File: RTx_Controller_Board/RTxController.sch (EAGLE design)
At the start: 73 parts

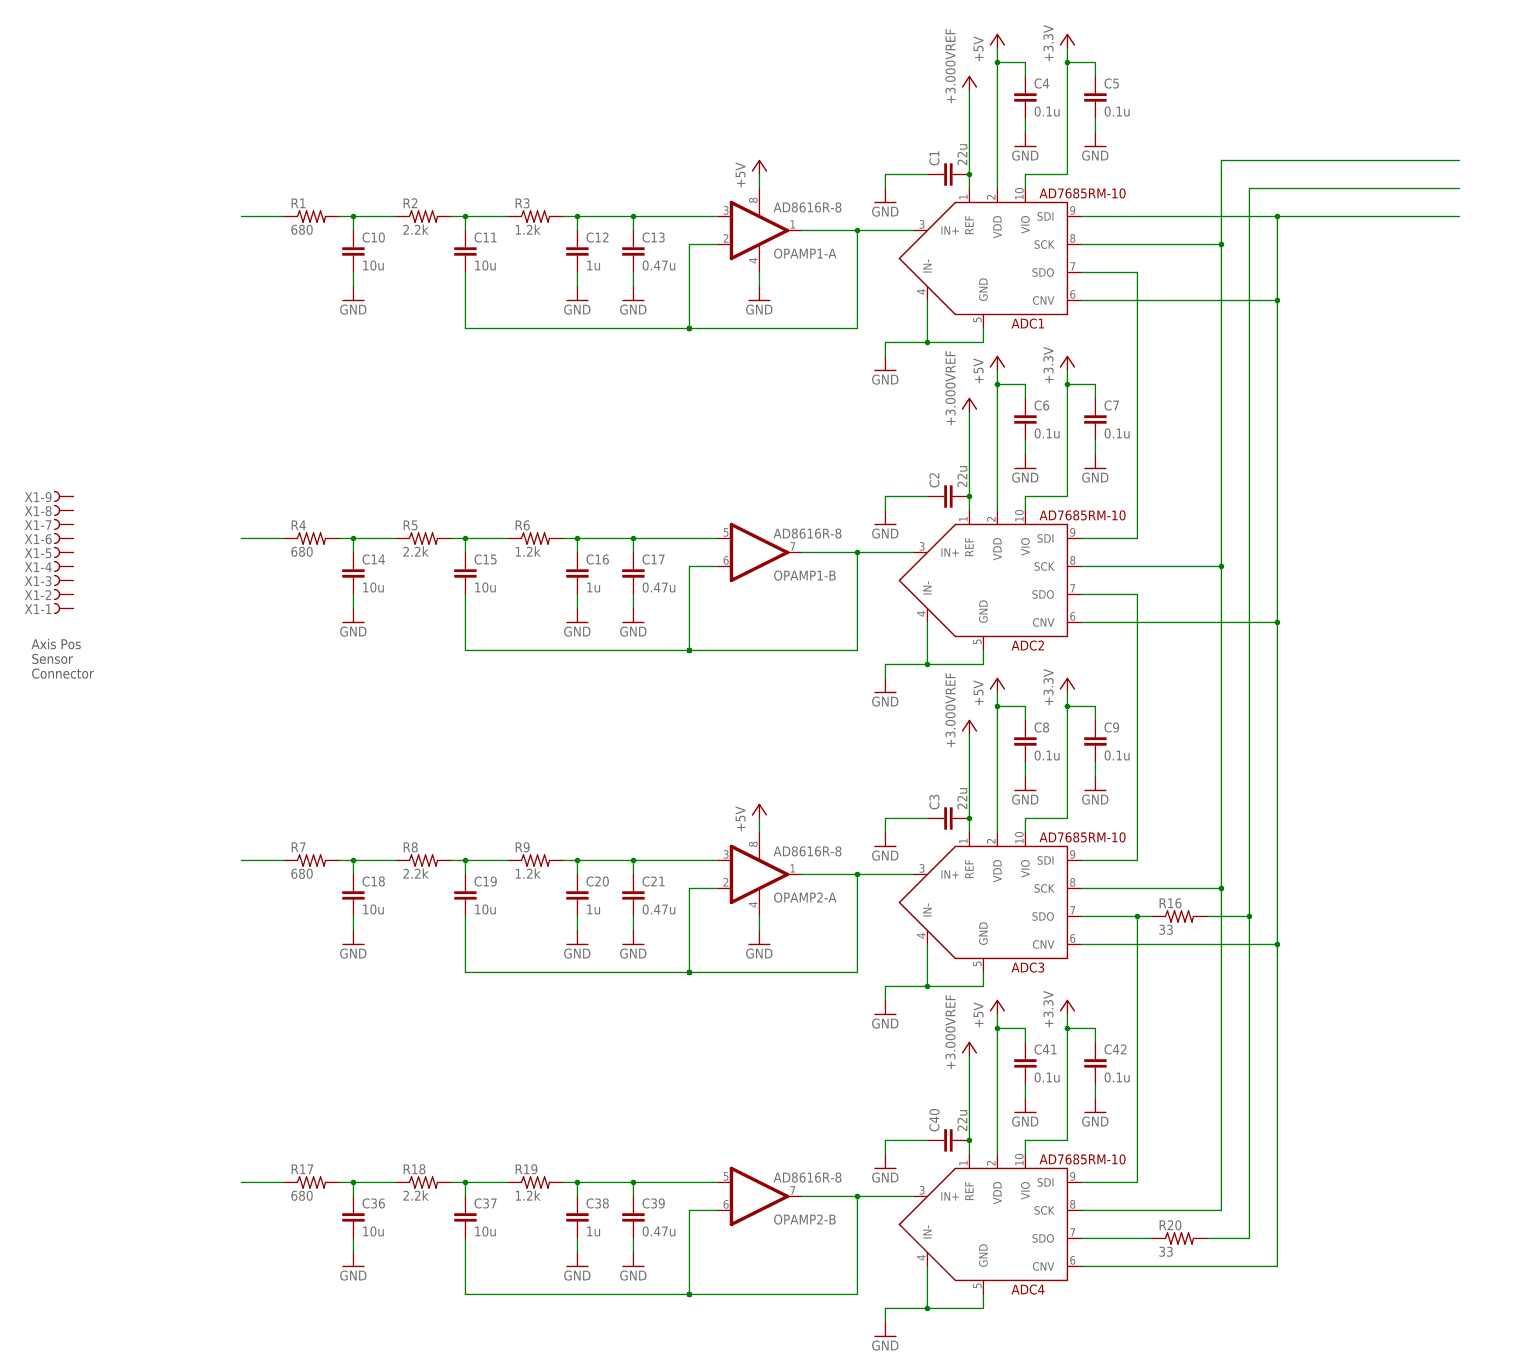
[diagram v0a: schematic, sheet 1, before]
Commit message: Changed ARef to 5.000V.
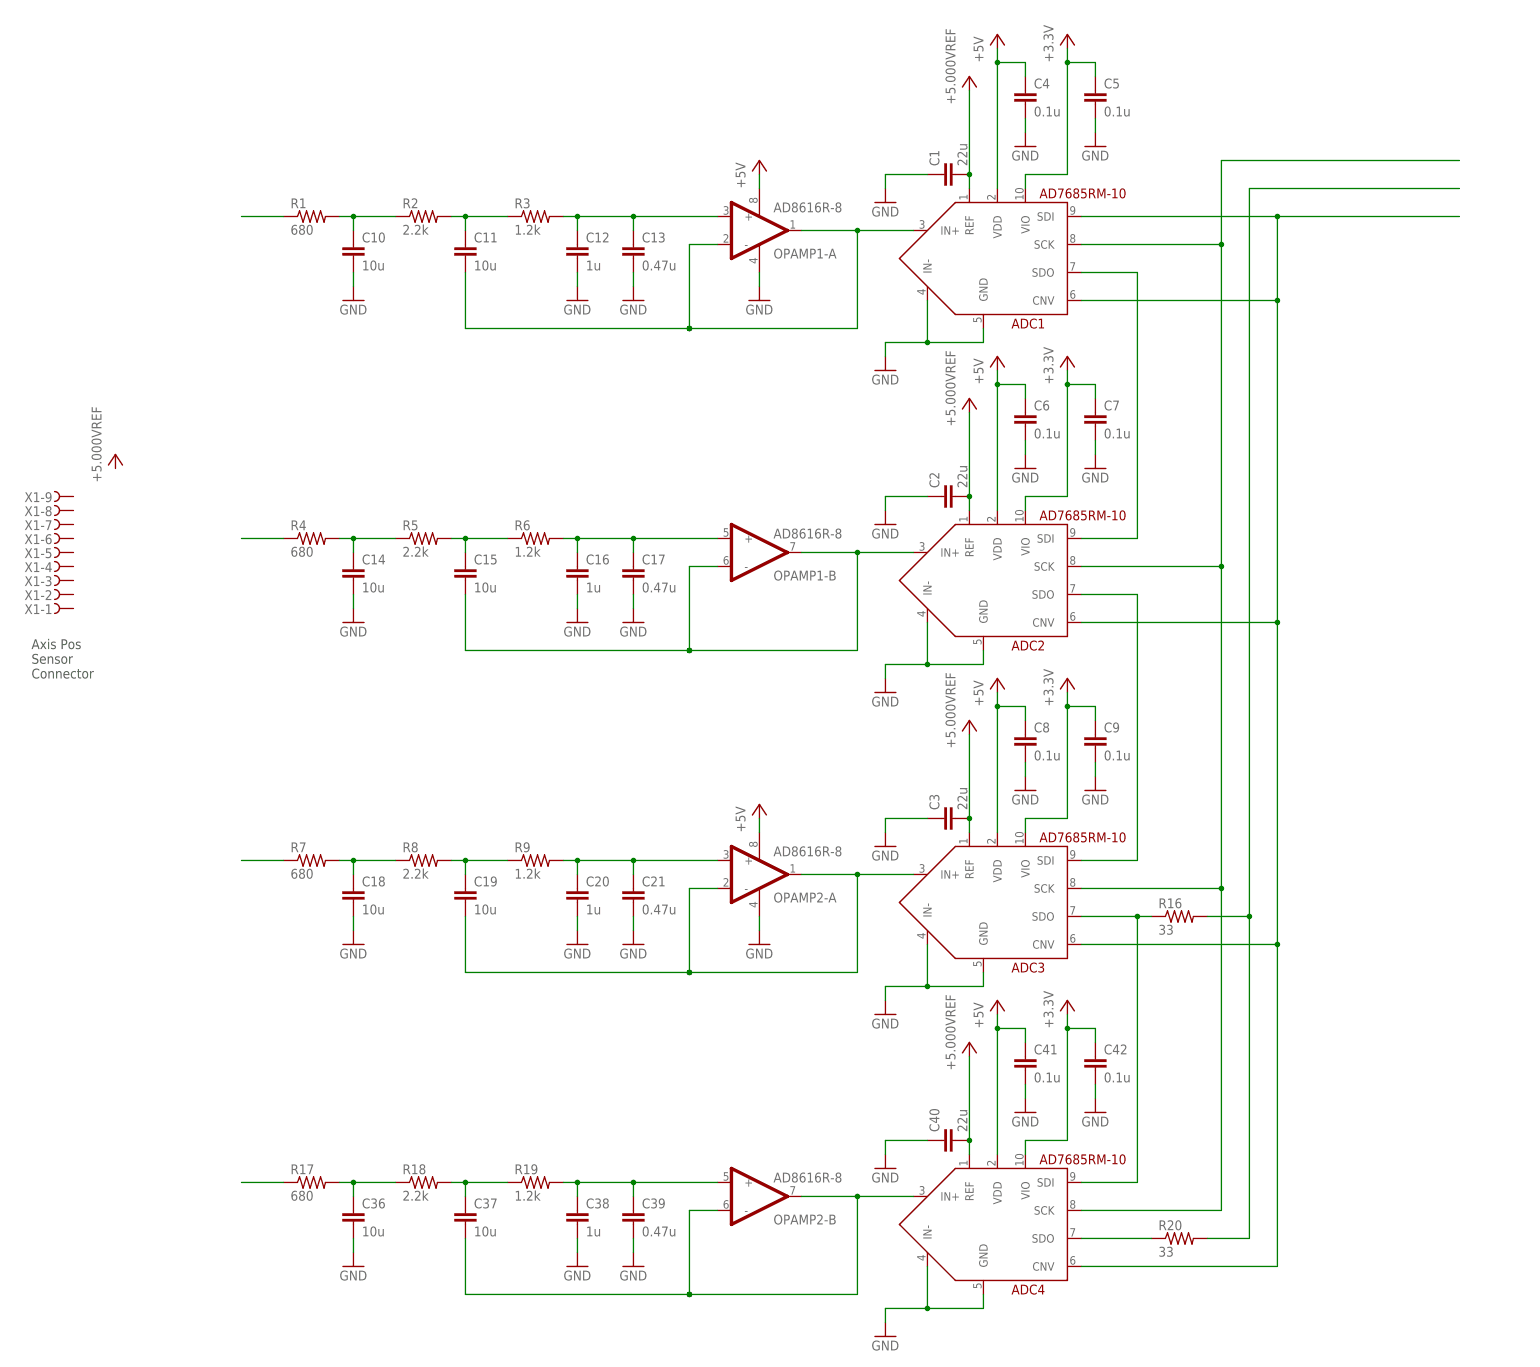
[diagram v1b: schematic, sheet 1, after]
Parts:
- removed REF1: ADR433RM-8, motorFeedback:ADR433RM-8
- added REF2: ADR435RM-8, motorFeedback:ADR435RM-8
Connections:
- removed net +3.000VREF: ADC1.REF@1, ADC2.REF@1, ADC3.REF@1, ADC4.REF@1, C1.2, C2.2, C23.1, C3.2, C40.2, R10.1, REF1.VOUT@6
- new net +18V: C24.1, C25.1, REF2.VIN@2
- new net +5.000VREF: ADC1.REF@1, ADC2.REF@1, ADC3.REF@1, ADC4.REF@1, C1.2, C2.2, C23.1, C3.2, C40.2, R10.1, REF2.VOUT@6
- net +5V: no longer C24.1, C25.1, REF1.VIN@2
- net ADC1_IN+: now also OPAMP1-A.-@2; no longer OPAMP1-A.-IN_A@2
- net ADC2_IN+: now also OPAMP1-B.-; no longer OPAMP1-B.-IN_B
- net ADC3_IN+: now also OPAMP2-A.-@2; no longer OPAMP2-A.-IN_A@2
- net ADC4_IN: now also OPAMP2-B.-; no longer OPAMP2-B.-IN_B
- net GND: now also REF2.GND@4; no longer REF1.GND@4
- net N$1: now also OPAMP1-A.+@3; no longer OPAMP1-A.+IN_A@3
- net N$12: now also OPAMP2-A.+@3; no longer OPAMP2-A.+IN_A@3
- net N$2: now also OPAMP1-B.+; no longer OPAMP1-B.+IN_B
- net N$3: now also OPAMP2-B.+; no longer OPAMP2-B.+IN_B

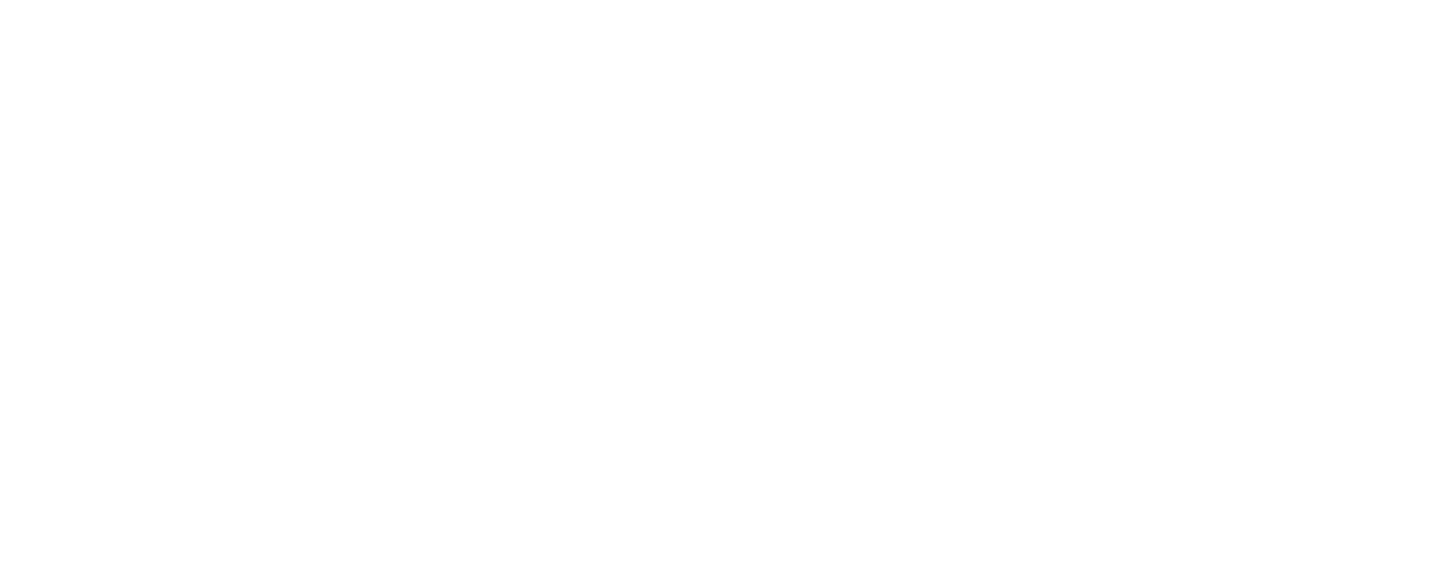
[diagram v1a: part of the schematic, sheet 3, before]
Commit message: Initial check-in datasheet for USB ESD protection. Added initial USB setup to schematic.
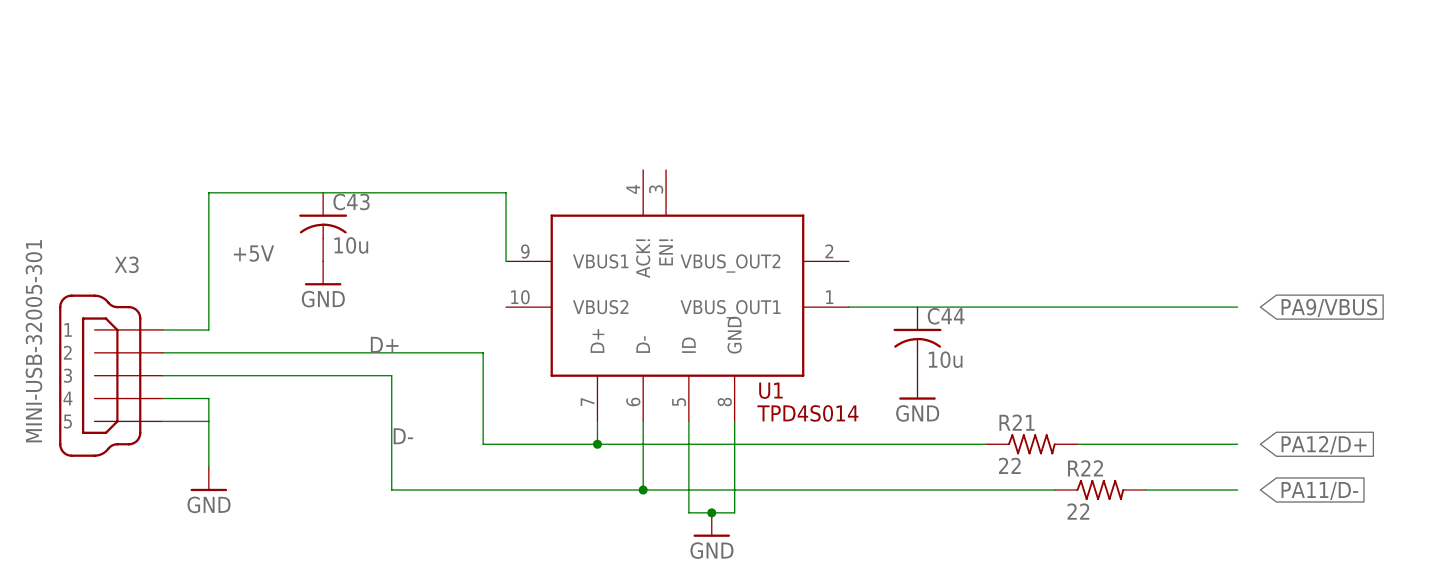
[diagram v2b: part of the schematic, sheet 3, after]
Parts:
- added C43, C44: 10u, rcl:C-USC0402
- added R21, R22: 22, rcl:R-US_R0402
- added U1: TPD4S014, rtx:TPD4S014
- added X3: MINI-USB-32005-301, con-cypressindustries:MINI-USB-32005-301
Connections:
- new net D+: R21.1, U1.D+, X3.2
- new net D-: R22.1, U1.D-, X3.3
- new net PA11/D-: R22.2
- new net PA12/D+: R21.2
- new net PA9/VBUS: C44.1, U1.VBUS_OUT1
- net +5V: now also C43.1, U1.VBUS1, X3.1
- net GND: now also C43.2, C44.2, U1.GND, U1.ID, X3.4, X3.5
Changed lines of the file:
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@@
 <part name="REF2" library="motorFeedback" deviceset="ADR435" device="RM-8"/>
 <part name="P+24" library="supply1" deviceset="+18V" device=""/>
+<part name="X3" library="con-cypressindustries" deviceset="MINI-USB-" device="32005-301"/>
+<part name="GND48" library="supply1" deviceset="GND" device=""/>
+<part name="U1" library="rtx" deviceset="TPD4S014" device=""/>
+<part name="GND49" library="supply1" deviceset="GND" device=""/>
+<part name="R21" library="rcl" deviceset="R-US_" device="R0402" value="22"/>
+<part name="R22" library="rcl" deviceset="R-US_" device="R0402" value="22"/>
+<part name="C43" library="rcl" deviceset="C-US" device="C0402" value="10u"/>
+<part name="C44" library="rcl" deviceset="C-US" device="C0402" value="10u"/>
+<part name="GND50" library="supply1" deviceset="GND" device=""/>
+<part name="GND51" library="supply1" deviceset="GND" device=""/>
 </parts>
 <sheets>
@@
 <instance part="X2" gate="-15" x="190.5" y="177.8" rot="R180"/>
 <instance part="U$3" gate="G$1" x="0" y="0"/>
+<instance part="X3" gate="G$1" x="83.82" y="83.82" rot="MR0"/>
+<instance part="GND48" gate="1" x="93.98" y="71.12" rot="MR0"/>
+<instance part="U1" gate="G$1" x="144.78" y="91.44"/>
+<instance part="GND49" gate="1" x="149.86" y="66.04" rot="MR0"/>
+<instance part="R21" gate="G$1" x="185.42" y="76.2"/>
+<instance part="R22" gate="G$1" x="193.04" y="71.12"/>
+<instance part="C43" gate="G$1" x="106.68" y="101.6"/>
+<instance part="C44" gate="G$1" x="172.72" y="88.9"/>
+<instance part="GND50" gate="1" x="106.68" y="93.98" rot="MR0"/>
+<instance part="GND51" gate="1" x="172.72" y="81.28" rot="MR0"/>
 </instances>
 <busses>
 </busses>
 <nets>
+<net name="GND" class="0">
+<segment>
+<pinref part="X3" gate="G$1" pin="4"/>
+<wire x1="88.9" y1="81.28" x2="93.98" y2="81.28" width="0.1524" layer="91"/>
+<wire x1="93.98" y1="81.28" x2="93.98" y2="78.74" width="0.1524" layer="91"/>
+<pinref part="X3" gate="G$1" pin="5"/>
+<wire x1="88.9" y1="78.74" x2="93.98" y2="78.74" width="0.1524" layer="91"/>
+<wire x1="93.98" y1="78.74" x2="93.98" y2="73.66" width="0.1524" layer="91"/>
+<pinref part="GND48" gate="1" pin="GND"/>
+</segment>
+<segment>
+<pinref part="U1" gate="G$1" pin="ID"/>
+<wire x1="147.32" y1="78.74" x2="147.32" y2="68.58" width="0.1524" layer="91"/>
+<wire x1="147.32" y1="68.58" x2="149.86" y2="68.58" width="0.1524" layer="91"/>
+<pinref part="U1" gate="G$1" pin="GND"/>
+<wire x1="149.86" y1="68.58" x2="152.4" y2="68.58" width="0.1524" layer="91"/>
+<wire x1="152.4" y1="68.58" x2="152.4" y2="78.74" width="0.1524" layer="91"/>
+<pinref part="GND49" gate="1" pin="GND"/>
+<junction x="149.86" y="68.58"/>
+</segment>
+<segment>
+<pinref part="C43" gate="G$1" pin="2"/>
+<pinref part="GND50" gate="1" pin="GND"/>
+</segment>
+<segment>
+<pinref part="C44" gate="G$1" pin="2"/>
+<pinref part="GND51" gate="1" pin="GND"/>
+</segment>
+</net>
+<net name="+5V" class="0">
+<segment>
+<pinref part="X3" gate="G$1" pin="1"/>
+<wire x1="88.9" y1="88.9" x2="93.98" y2="88.9" width="0.1524" layer="91"/>
+<wire x1="93.98" y1="88.9" x2="93.98" y2="104.14" width="0.1524" layer="91"/>
+<wire x1="93.98" y1="104.14" x2="106.68" y2="104.14" width="0.1524" layer="91"/>
+<label x="96.52" y="96.52" size="1.778" layer="95"/>
+<pinref part="C43" gate="G$1" pin="1"/>
+<pinref part="U1" gate="G$1" pin="VBUS1"/>
+<wire x1="106.68" y1="104.14" x2="127" y2="104.14" width="0.1524" layer="91"/>
+<wire x1="127" y1="104.14" x2="127" y2="96.52" width="0.1524" layer="91"/>
+</segment>
+</net>
+<net name="D+" class="0">
+<segment>
+<pinref part="X3" gate="G$1" pin="2"/>
+<wire x1="88.9" y1="86.36" x2="124.46" y2="86.36" width="0.1524" layer="91"/>
+<wire x1="124.46" y1="86.36" x2="124.46" y2="76.2" width="0.1524" layer="91"/>
+<pinref part="U1" gate="G$1" pin="D+"/>
+<wire x1="124.46" y1="76.2" x2="137.16" y2="76.2" width="0.1524" layer="91"/>
+<wire x1="137.16" y1="78.74" x2="137.16" y2="76.2" width="0.1524" layer="91"/>
+<wire x1="137.16" y1="76.2" x2="180.34" y2="76.2" width="0.1524" layer="91"/>
+<junction x="137.16" y="76.2"/>
+<label x="111.76" y="86.36" size="1.778" layer="95"/>
+<pinref part="R21" gate="G$1" pin="1"/>
+</segment>
+</net>
+<net name="D-" class="0">
+<segment>
+<pinref part="X3" gate="G$1" pin="3"/>
+<wire x1="88.9" y1="83.82" x2="114.3" y2="83.82" width="0.1524" layer="91"/>
+<wire x1="114.3" y1="83.82" x2="114.3" y2="71.12" width="0.1524" layer="91"/>
+<pinref part="U1" gate="G$1" pin="D-"/>
+<wire x1="114.3" y1="71.12" x2="142.24" y2="71.12" width="0.1524" layer="91"/>
+<wire x1="142.24" y1="78.74" x2="142.24" y2="71.12" width="0.1524" layer="91"/>
+<wire x1="142.24" y1="71.12" x2="187.96" y2="71.12" width="0.1524" layer="91"/>
+<junction x="142.24" y="71.12"/>
+<label x="114.3" y="76.2" size="1.778" layer="95"/>
+<pinref part="R22" gate="G$1" pin="1"/>
+</segment>
+</net>
+<net name="PA9/VBUS" class="0">
+<segment>
+<pinref part="U1" gate="G$1" pin="VBUS_OUT1"/>
+<pinref part="C44" gate="G$1" pin="1"/>
+<wire x1="165.1" y1="91.44" x2="172.72" y2="91.44" width="0.1524" layer="91"/>
+<wire x1="172.72" y1="91.44" x2="208.28" y2="91.44" width="0.1524" layer="91"/>
+<label x="210.82" y="91.44" size="1.778" layer="95" xref="yes"/>
+</segment>
+</net>
+<net name="PA12/D+" class="0">
+<segment>
+<pinref part="R21" gate="G$1" pin="2"/>
+<wire x1="190.5" y1="76.2" x2="208.28" y2="76.2" width="0.1524" layer="91"/>
+<label x="210.82" y="76.2" size="1.778" layer="95" xref="yes"/>
+</segment>
+</net>
+<net name="PA11/D-" class="0">
+<segment>
+<pinref part="R22" gate="G$1" pin="2"/>
+<wire x1="198.12" y1="71.12" x2="208.28" y2="71.12" width="0.1524" layer="91"/>
+<label x="210.82" y="71.12" size="1.778" layer="95" xref="yes"/>
+</segment>
+</net>
 </nets>
 </sheet>
